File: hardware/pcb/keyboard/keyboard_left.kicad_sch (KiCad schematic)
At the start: 37 parts, among them J1 SM04B-SRSS-TB, J2 PJ320D, J3 HRO_TYPE-C-31-M-12, J4 FH34SRJ-12S-0.5SH, SW29 PTS845, U3 PRTR5V0U2X, U4 XC6220B331MR-G, U5 STM32G431KBTx, U6 CH334R, Y1 8MHz, Y2 12MHz

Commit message: temp
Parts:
- U6: footprint Package_SO:QSOP-16_3.9x4.9mm_P0.635mm -> PCM_Package_SO_AKL:QSOP-16_3.9x4.9mm_P0.635mm
- Y1: value 8MHz -> 8MHz 10pF
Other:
- note added: "STM32G431KBTx"
- note removed: "STM32G0B1KxT Series"

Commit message: rev2
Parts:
- removed C11, C14: 1uF, PCM_Capacitor_SMD_AKL:C_0603_1608Metric, symbol Device:C
- removed C12, C13: 10pF, PCM_Capacitor_SMD_AKL:C_0603_1608Metric, symbol Device:C
- removed U6: CH334R, PCM_Package_SO_AKL:QSOP-16_3.9x4.9mm_P0.635mm, symbol wch_mcu_peripheral:CH334R
- removed Y2: 12MHz, PCM_Crystal_Handsoldering_AKL:Crystal_SMD_2520-4Pin_2.5x2.0mm, symbol Device:Crystal_GND24_Small
- J1: value SM04B-SRSS-TB -> SM03B-SRSS-TB; footprint Connector_JST:JST_SH_SM04B-SRSS-TB_1x04-1MP_P1.00mm_Horizontal -> Connector_JST:JST_SH_SM03B-SRSS-TB_1x03-1MP_P1.00mm_Horizontal; symbol Connector_Generic_MountingPin:Conn_01x04_MountingPin -> Connector_Generic_MountingPin:Conn_01x03_MountingPin
- renumbered C20 to C8, C21 to C9, R9 to R1, R9 to R2, R9 to R3, R9 to R4, R9 to R8
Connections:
- net DM4 is gone; now on net +5V: J4.2 (Pin_2)
- net DP4 is gone; now on net +5V: J4.3 (Pin_3)
- net UP_D+ is gone; now on net D+: J3.A6 (D+), J3.B6 (D+), U3.3 (I/O2)
- net UP_D- is gone; now on net D-: J3.A7 (D-), J3.B7 (D-), U3.2 (I/O1)
- net +3V3: no longer J1.1 (Pin_1), J4.4 (Pin_4)
- net ACCS_3: no longer R1.1, R4.2
- net GND: now also J1.2 (Pin_2), J4.9 (Pin_9), TP1.3 (Pin_3); no longer J1.4 (Pin_4), J1.MP (MountPin), TP1.4 (Pin_4)
- net SWCLK: now also J1.1 (Pin_1), TP1.2 (Pin_2); no longer J1.3 (Pin_3), TP1.3 (Pin_3)
- net SWDIO: now also J1.3 (Pin_3), TP1.4 (Pin_4); no longer J1.2 (Pin_2), TP1.2 (Pin_2)
- net VBUS: no longer J4.1 (Pin_1)
- net ACCS_5 renamed PB6
- net PB6: now also R1.1, R4.2; no longer J4.9 (Pin_9)
- net MCU_D+ renamed D+
- net MCU_D- renamed D-
- no-connect marks 8 -> 10

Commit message: init memory
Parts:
- removed J4: FH34SRJ-12S-0.5SH, ec_parts:HRS_FH34SRJ-12S-0.5SH(50), symbol Connector_Generic_MountingPin:Conn_01x12_MountingPin
- added C14: 10n, PCM_Capacitor_SMD_AKL:C_0603_1608Metric, symbol Device:C
- added J4: HRS_FH34SRJ-06S-0.5SH(50), ec_parts:CONN6x1_FH34SRJ-6S-0.5SH50_HIR, symbol Connector_Generic_MountingPin:Conn_01x06_MountingPin
- added U6: 24FC01T-I/OT, SOT-23-5_2P9X1P6_MCH, symbol 24FC01T-I/OT:24FC01T-I_OT
- SW29: symbol Switch:SW_Push -> ec_parts:SW_Push
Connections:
- net +3V3: now also C14.1
- net ACCS_1: now also J4.5 (Pin_5)
- net ACCS_2: now also J4.4 (Pin_4)
- net ACCS_3: now also J4.3 (Pin_3)
- net ACCS_4: now also J4.2 (Pin_2)
- net GND: now also J4.1 (Pin_1), U6.2 (VSS), U6.5 (WP)
- net ACCS_6 renamed I2C1_SDA
- net I2C1_SDA: now also U6.3 (SDA)
- net ACCS_7 renamed I2C1_SCL
- net I2C1_SCL: now also U6.1 (SCL)
- new net: C14.2, U6.4 (VCC)
- no-connect marks 10 -> 8

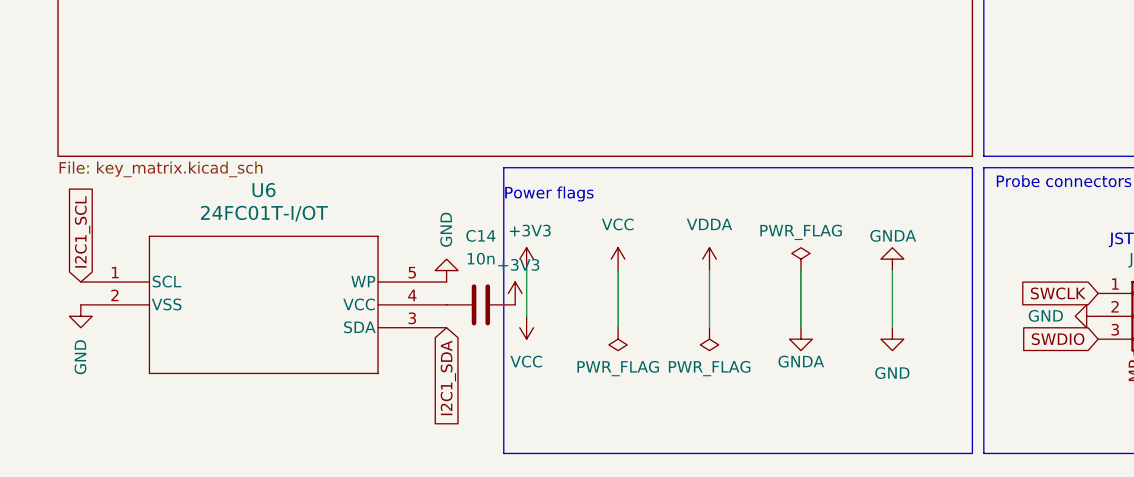
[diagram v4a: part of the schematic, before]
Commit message: add pull up register for I2C.
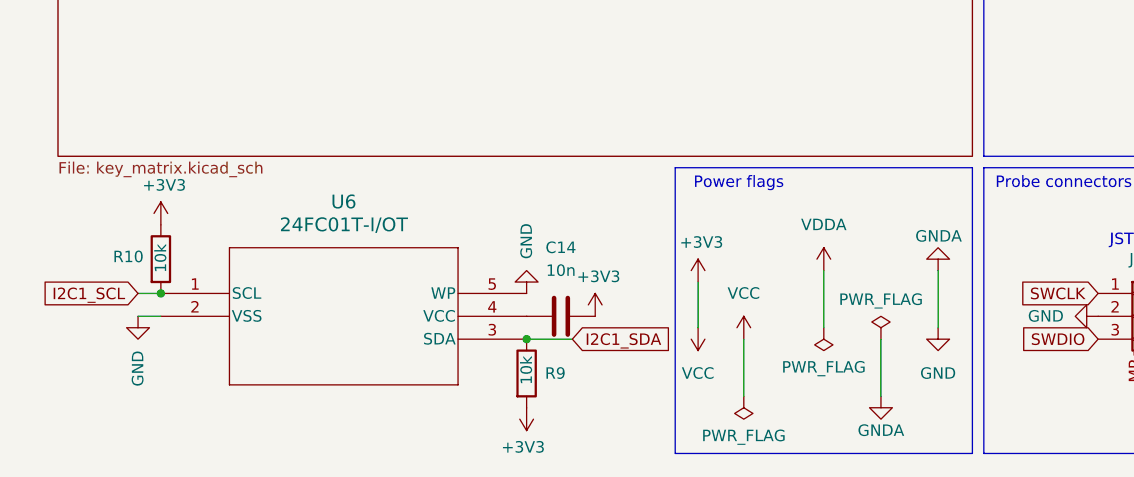
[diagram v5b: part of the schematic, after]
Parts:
- added R10, R9: 10k, PCM_Resistor_SMD_AKL:R_0603_1608Metric, symbol Device:R
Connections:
- net +3V3: now also R10.1, R9.2
- net I2C1_SCL: now also R10.2
- net I2C1_SDA: now also R9.1
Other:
- moved on the sheet: C14, U6

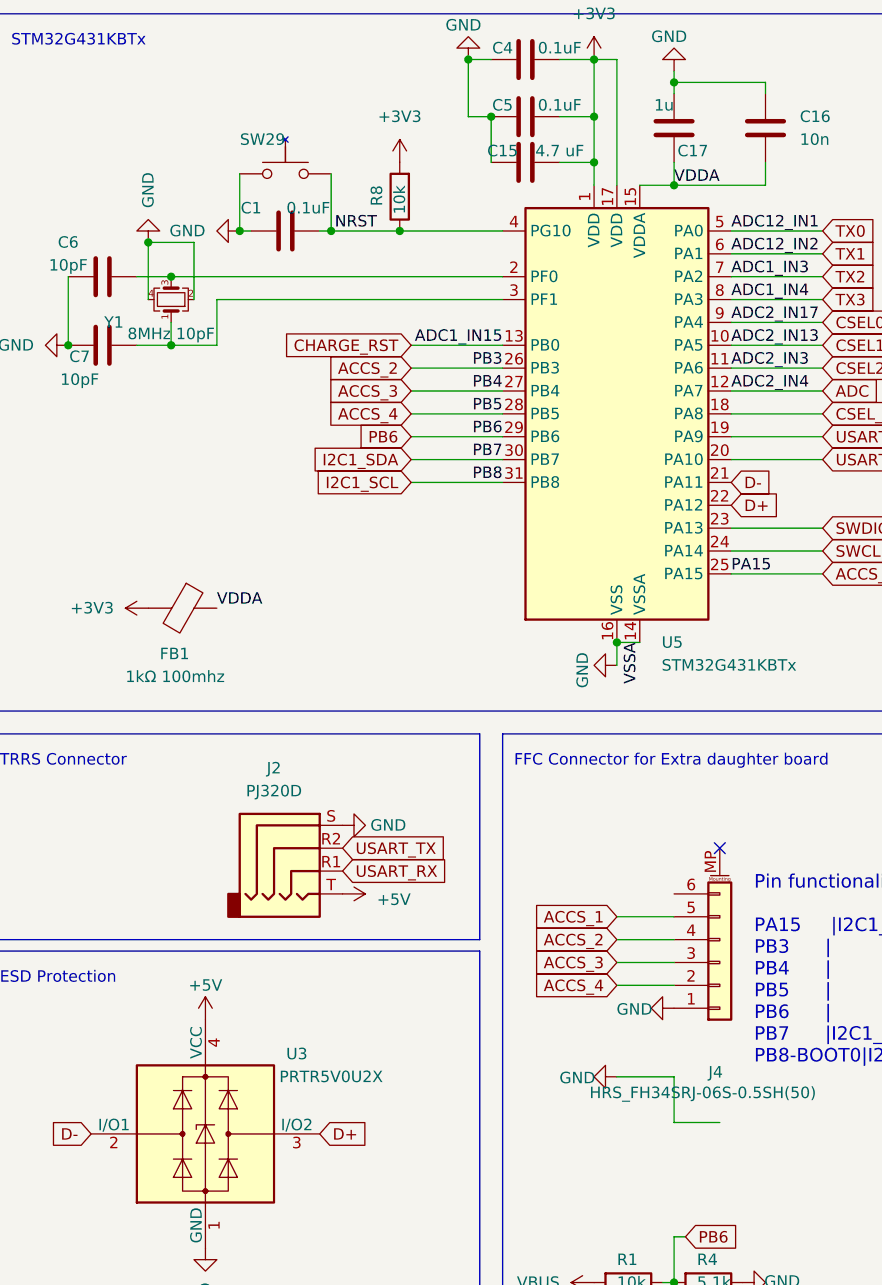
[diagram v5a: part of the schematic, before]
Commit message: fix acc connection.
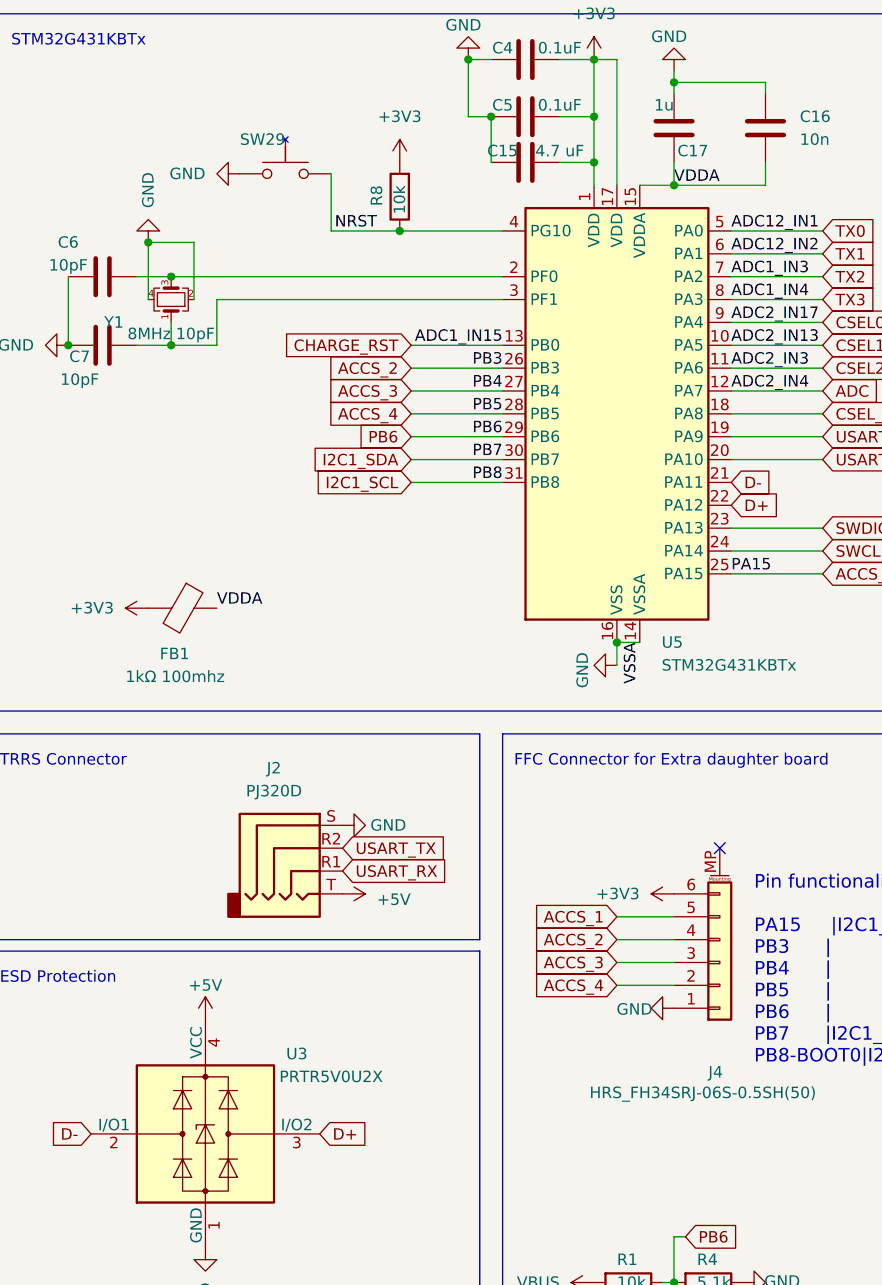
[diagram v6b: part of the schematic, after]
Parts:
- removed C1: 0.1uF, PCM_Capacitor_SMD_AKL:C_0603_1608Metric, symbol Device:C
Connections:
- net +3V3: now also J4.6 (Pin_6)
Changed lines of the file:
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@@
 	)
 	(junction
-		(at 153.67 38.1)
-		(diameter 0)
-		(color 0 0 0 0)
-	)
-	(junction
 		(at 64.77 184.15)
 		(diameter 0)
@@
 	)
 	(junction
-		(at 143.51 38.1)
-		(diameter 0)
-		(color 0 0 0 0)
-	)
-	(junction
 		(at 171.45 25.4)
 		(diameter 0)
@@
 	(wire
 		(pts
-			(xy 191.77 132.08) (xy 185.42 132.08)
-		)
-		(stroke
-			(width 0)
-			(type default)
-		)
-	)
-	(wire
-		(pts
 			(xy 273.05 26.67) (xy 270.51 26.67)
 		)
@@
 	(wire
 		(pts
-			(xy 144.78 38.1) (xy 143.51 38.1)
-		)
-		(stroke
-			(width 0)
-			(type default)
-		)
-	)
-	(wire
-		(pts
-			(xy 143.51 38.1) (xy 143.51 31.75)
-		)
-		(stroke
-			(width 0)
-			(type default)
-		)
-	)
-	(wire
-		(pts
 			(xy 80.01 30.48) (xy 80.01 31.75)
 		)
@@
 	(wire
 		(pts
-			(xy 191.77 137.16) (xy 191.77 132.08)
-		)
-		(stroke
-			(width 0)
-			(type default)
-		)
-	)
-	(wire
-		(pts
 			(xy 58.42 25.4) (xy 58.42 31.75)
 		)
@@
 	(wire
 		(pts
-			(xy 152.4 38.1) (xy 153.67 38.1)
-		)
-		(stroke
-			(width 0)
-			(type default)
-		)
-	)
-	(wire
-		(pts
 			(xy 201.93 30.48) (xy 201.93 33.02)
 		)
@@
 	(wire
 		(pts
-			(xy 196.85 137.16) (xy 191.77 137.16)
-		)
-		(stroke
-			(width 0)
-			(type default)
-		)
-	)
-	(wire
-		(pts
 			(xy 68.58 51.435) (xy 68.58 50.8)
 		)
@@
 	)
 	(symbol
-		(lib_id "nrfmicro-rescue:GND")
-		(at 185.42 132.08 270)
-		(unit 1)
-		(exclude_from_sim no)
-		(in_bom yes)
-		(on_board yes)
-		(dnp no)
-		(property "Reference" "#PWR015"
-			(at 179.07 132.08 0)
-			(effects
-				(font
-					(size 1.27 1.27)
-				)
-				(hide yes)
-			)
-		)
-		(property "Value" "GND"
-			(at 181.0258 132.207 90)
-			(effects
-				(font
-					(size 1.27 1.27)
-				)
-			)
-		)
-		(property "Footprint" ""
-			(at 185.42 132.08 0)
-			(effects
-				(font
-					(size 1.27 1.27)
-				)
-				(hide yes)
-			)
-		)
-		(property "Datasheet" ""
-			(at 185.42 132.08 0)
-			(effects
-				(font
-					(size 1.27 1.27)
-				)
-				(hide yes)
-			)
-		)
-		(property "Description" ""
-			(at 185.42 132.08 0)
-			(effects
-				(font
-					(size 1.27 1.27)
-				)
-				(hide yes)
-			)
-		)
-		(pin "1"
-		)
-		(instances
-			(project "esp32_hub_right"
-				(path "/5de5818a-c52c-4286-93c9-eb63836c2db5"
-					(reference "#PWR029")
-					(unit 1)
-				)
-			)
-			(project "keyboard_left"
-				(path "/852dabbf-de45-4470-8176-59d37a754407"
-					(reference "#PWR015")
-					(unit 1)
-				)
-			)
-			(project "nrfmicro"
-				(path "/bfc0aadc-38cf-466e-a642-68fdc3138c78"
-					(reference "#PWR0119")
-					(unit 1)
-				)
-			)
-		)
-	)
-	(symbol
 		(lib_id "power:GND")
 		(at 191.77 20.32 180)
@@
 	)
 	(symbol
+		(lib_id "power:GND")
+		(at 143.51 31.75 270)
+		(unit 1)
+		(exclude_from_sim no)
+		(in_bom yes)
+		(on_board yes)
+		(dnp no)
+		(property "Reference" "#PWR025"
+			(at 137.16 31.75 0)
+			(effects
+				(font
+					(size 1.27 1.27)
+				)
+				(hide yes)
+			)
+		)
+		(property "Value" "GND"
+			(at 139.7 31.75 90)
+			(effects
+				(font
+					(size 1.27 1.27)
+				)
+				(justify right)
+			)
+		)
+		(property "Footprint" ""
+			(at 143.51 31.75 0)
+			(effects
+				(font
+					(size 1.27 1.27)
+				)
+				(hide yes)
+			)
+		)
+		(property "Datasheet" ""
+			(at 143.51 31.75 0)
+			(effects
+				(font
+					(size 1.27 1.27)
+				)
+				(hide yes)
+			)
+		)
+		(property "Description" ""
+			(at 143.51 31.75 0)
+			(effects
+				(font
+					(size 1.27 1.27)
+				)
+				(hide yes)
+			)
+		)
+		(pin "1"
+		)
+		(instances
+			(project "keyboard_left"
+				(path "/852dabbf-de45-4470-8176-59d37a754407"
+					(reference "#PWR025")
+					(unit 1)
+				)
+			)
+		)
+	)
+	(symbol
 		(lib_id "power:GNDA")
 		(at 110.49 176.53 180)
@@
 	)
 	(symbol
+		(lib_id "power:+3.3V")
+		(at 191.77 111.76 90)
+		(unit 1)
+		(exclude_from_sim no)
+		(in_bom yes)
+		(on_board yes)
+		(dnp no)
+		(fields_autoplaced yes)
+		(property "Reference" "#PWR015"
+			(at 195.58 111.76 0)
+			(effects
+				(font
+					(size 1.27 1.27)
+				)
+				(hide yes)
+			)
+		)
+		(property "Value" "+3V3"
+			(at 187.96 111.7599 90)
+			(effects
+				(font
+					(size 1.27 1.27)
+				)
+				(justify left)
+			)
+		)
+		(property "Footprint" ""
+			(at 191.77 111.76 0)
+			(effects
+				(font
+					(size 1.27 1.27)
+				)
+				(hide yes)
+			)
+		)
+		(property "Datasheet" ""
+			(at 191.77 111.76 0)
+			(effects
+				(font
+					(size 1.27 1.27)
+				)
+				(hide yes)
+			)
+		)
+		(property "Description" ""
+			(at 191.77 111.76 0)
+			(effects
+				(font
+					(size 1.27 1.27)
+				)
+				(hide yes)
+			)
+		)
+		(pin "1"
+		)
+		(instances
+			(project "keyboard_left"
+				(path "/852dabbf-de45-4470-8176-59d37a754407"
+					(reference "#PWR015")
+					(unit 1)
+				)
+			)
+		)
+	)
+	(symbol
 		(lib_name "GNDPWR_1")
 		(lib_id "power:GNDPWR")
@@
 	)
 	(symbol
-		(lib_id "power:GND")
-		(at 143.51 38.1 270)
-		(unit 1)
-		(exclude_from_sim no)
-		(in_bom yes)
-		(on_board yes)
-		(dnp no)
-		(property "Reference" "#PWR046"
-			(at 137.16 38.1 0)
-			(effects
-				(font
-					(size 1.27 1.27)
-				)
-				(hide yes)
-			)
-		)
-		(property "Value" "GND"
-			(at 139.7 38.1 90)
-			(effects
-				(font
-					(size 1.27 1.27)
-				)
-				(justify right)
-			)
-		)
-		(property "Footprint" ""
-			(at 143.51 38.1 0)
-			(effects
-				(font
-					(size 1.27 1.27)
-				)
-				(hide yes)
-			)
-		)
-		(property "Datasheet" ""
-			(at 143.51 38.1 0)
-			(effects
-				(font
-					(size 1.27 1.27)
-				)
-				(hide yes)
-			)
-		)
-		(property "Description" ""
-			(at 143.51 38.1 0)
-			(effects
-				(font
-					(size 1.27 1.27)
-				)
-				(hide yes)
-			)
-		)
-		(pin "1"
-		)
-		(instances
-			(project "keyboard_left"
-				(path "/852dabbf-de45-4470-8176-59d37a754407"
-					(reference "#PWR046")
-					(unit 1)
-				)
-			)
-			(project "EC60-Rev_1_1"
-				(path "/e63e39d7-6ac0-4ffd-8aa3-1841a4541b55"
-					(reference "#PWR020")
-					(unit 1)
-				)
-			)
-		)
-	)
-	(symbol
 		(lib_id "power:VBUS")
 		(at 58.42 25.4 0)
@@
 					(unit 1)
 				)
-			)
-		)
-	)
-	(symbol
-		(lib_id "Device:C")
-		(at 148.59 38.1 90)
-		(mirror x)
-		(unit 1)
-		(exclude_from_sim no)
-		(in_bom yes)
-		(on_board yes)
-		(dnp no)
-		(property "Reference" "C1"
-			(at 144.78 35.56 90)
-			(effects
-				(font
-					(size 1.27 1.27)
-				)
-			)
-		)
-		(property "Value" "0.1uF"
-			(at 151.13 35.56 90)
-			(effects
-				(font
-					(size 1.27 1.27)
-				)
-			)
-		)
-		(property "Footprint" "PCM_Capacitor_SMD_AKL:C_0603_1608Metric"
-			(at 152.4 39.0652 0)
-			(effects
-				(font
-					(size 1.27 1.27)
-				)
-				(hide yes)
-			)
-		)
-		(property "Datasheet" "~"
-			(at 148.59 38.1 0)
-			(effects
-				(font
-					(size 1.27 1.27)
-				)
-				(hide yes)
-			)
-		)
-		(property "Description" ""
-			(at 148.59 38.1 0)
-			(effects
-				(font
-					(size 1.27 1.27)
-				)
-				(hide yes)
-			)
-		)
-		(property "LCSC" "C307331"
-			(at 148.59 38.1 0)
-			(effects
-				(font
-					(size 1.27 1.27)
-				)
-				(hide yes)
-			)
-		)
-		(pin "1"
-		)
-		(pin "2"
-		)
-		(instances
-			(project "keyboard_left"
-				(path "/852dabbf-de45-4470-8176-59d37a754407"
-					(reference "C1")
-					(unit 1)
-				)
-			)
-			(project "EC60-Rev_1_1"
-				(path "/e63e39d7-6ac0-4ffd-8aa3-1841a4541b55"
-					(reference "C5")
-					(unit 1)
-				)

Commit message: update schema.
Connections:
- net ACCS_1 renamed PA15
- net ACCS_2 renamed PB3
- net ACCS_3 renamed PB4
- net ACCS_4 renamed PB5
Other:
- note added: "Pin functionalities. PA15 |I2C1_SCL |SPI1_NSS |SPI3_NSS | |USART2_RX PB3 | |SPI1_SCK |SPI3_SCK | |USART2_TX PB4 | |SPI1_MISO|SPI3_MISO| |USART2_RX PB5 | |SPI1_MOSI|SPI3_MOSI| |USART2_CK"
- note removed: "Pin functionalities. PA15 |I2C1_SCL |SPI1_NSS |SPI3_NSS | |USART2_RX PB3 | |SPI1_SCK |SPI3_SCK | |USART2_TX PB4 | |SPI1_MISO|SPI3_MISO| |USART2_RX PB5 | |SPI1_MOSI|SPI3_MOSI| |USART2_CK PB6 | | | |USART1_TX| PB7 |I2C1_SDA | | |USART1_RX| PB8-BOOT0|I2C1_SCL | | |"
- company: (none) -> https://github.com/daehyeok/Corne_EEC
- moved on the sheet: C14, R10, R9, U6

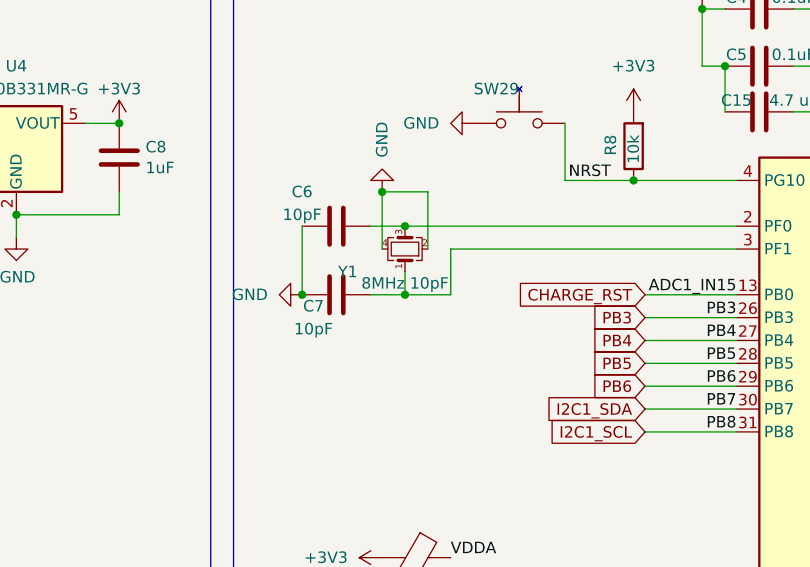
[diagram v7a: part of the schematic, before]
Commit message: Change crystal
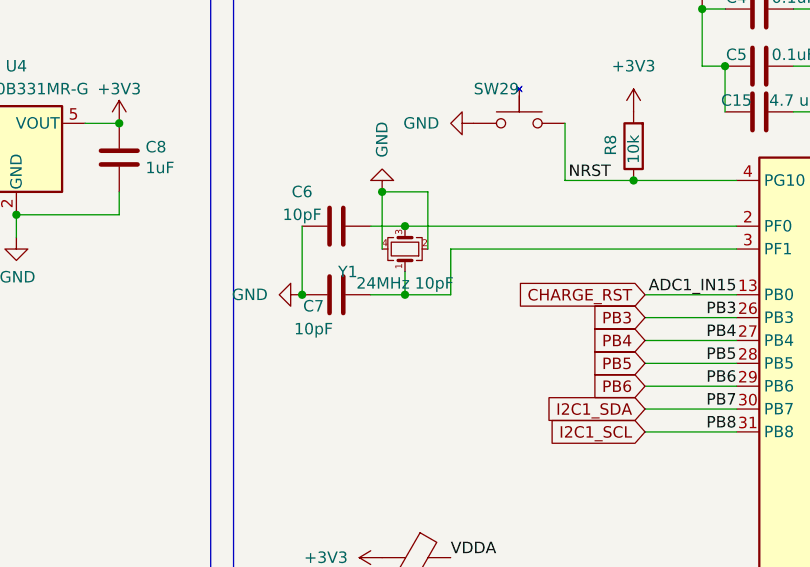
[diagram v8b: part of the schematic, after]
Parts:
- Y1: value 8MHz 10pF -> 24MHz 10pF
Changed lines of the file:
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@@
 			)
 		)
-		(property "Value" "8MHz 10pF"
+		(property "Value" "24MHz 10pF"
 			(at 135.89 49.53 90)
 			(effects
